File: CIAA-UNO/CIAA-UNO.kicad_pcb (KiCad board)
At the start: 2 copper layers, 53.3 x 68.6 mm, 42 parts, among them CON1 BARREL_JACK, J1 USB_OTG, J2 SWD, P1 Power Header, P2 Analog Header, P3 Digital Header 02, P4 Digital Header 01, Q1 FDN340P, SW1 reset, SW2 reset, U1 LD1117S50TR, U2 LMV358IDGKR, U3 LP2985-33DBVR, U4 USBLC6-2, U5 EFM32HG-48LQFP

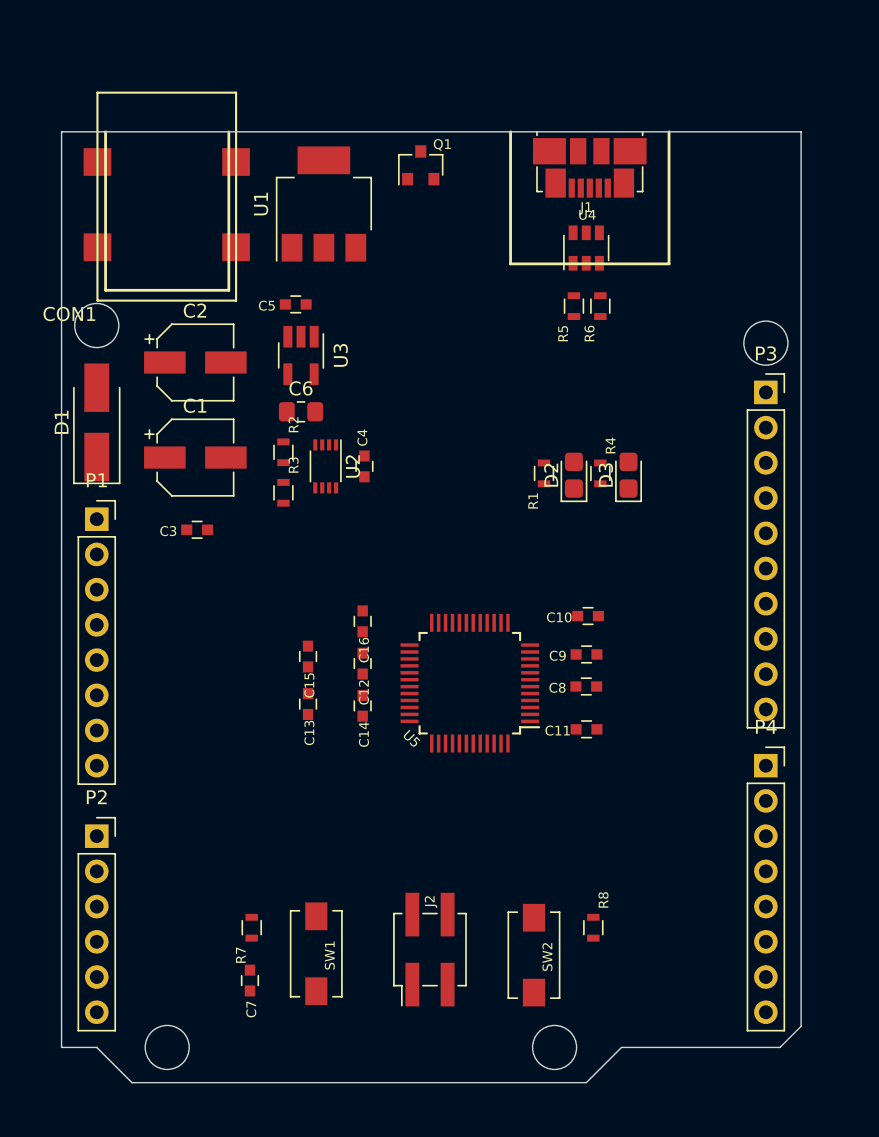
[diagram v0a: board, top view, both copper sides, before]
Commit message: Diseño del PCB
Faltan fiduciales, comentarios y rótulo.
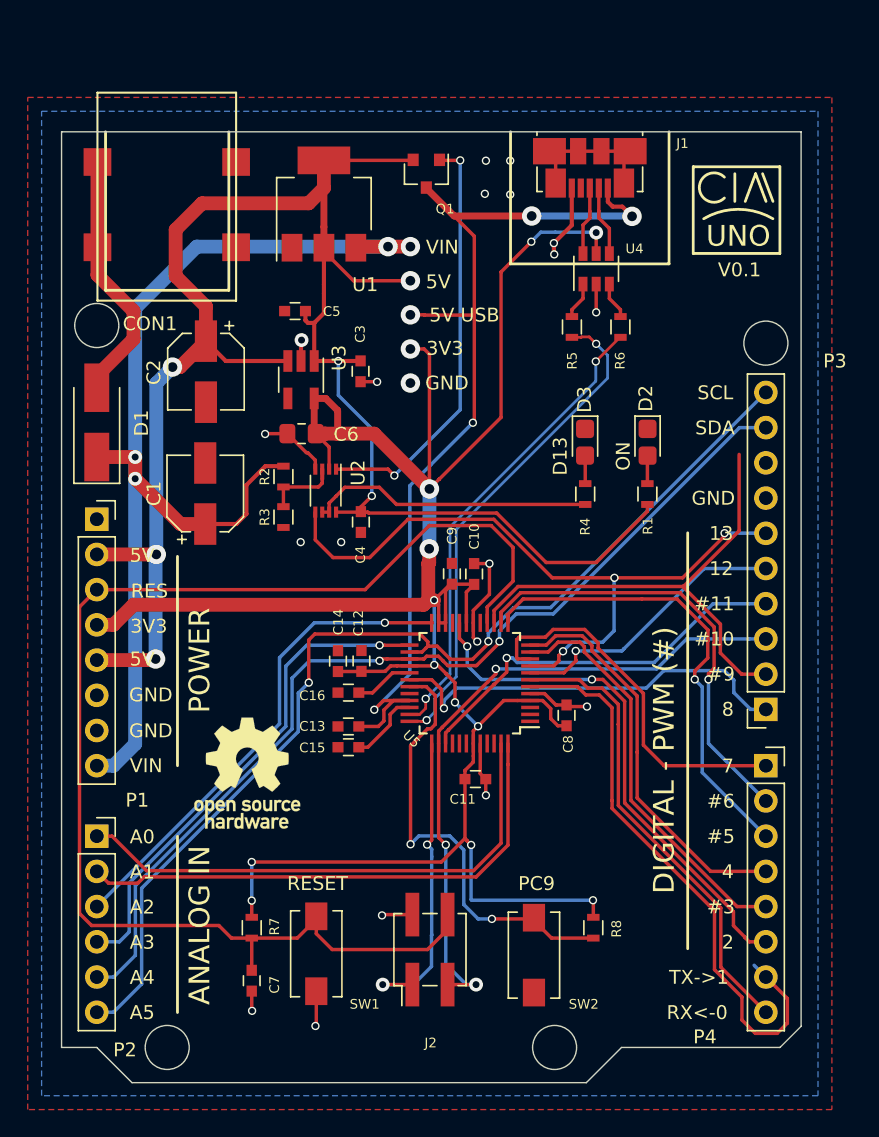
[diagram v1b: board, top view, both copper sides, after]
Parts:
- added REF**: OSHW-Logo_7.5x8mm_SilkScreen, Symbol:OSHW-Logo_7.5x8mm_SilkScreen, F.Cu at (104.8, 76.7)
- moved P3 22.9 mm to (142.2, 72.1), turned to 180 degrees
- moved C3 16.4 mm to (113.0, 47.8), turned to 270 degrees
- moved C9 11.3 mm to (119.6, 62.4), turned to 90 degrees
- moved C11 8.79 mm to (121.3, 77.2), turned to 180 degrees
- moved C10 8.76 mm to (121.2, 62.4), turned to 270 degrees
- moved R1 7.60 mm to (133.7, 56.6)
- moved C15 7.16 mm to (112.1, 74.9), turned to 180 degrees
- moved D2 5.82 mm to (133.7, 52.9), turned to 270 degrees
- moved C16 5.25 mm to (112.1, 70.9), turned to 180 degrees
- moved C4 4.02 mm to (113.0, 58.6), turned to 90 degrees
- moved D3 3.93 mm to (129.2, 52.9), turned to 270 degrees
- moved C14 3.68 mm to (111.4, 68.7)
- moved C13 3.33 mm to (112.1, 73.4), turned to 180 degrees
- moved C1 2.69 mm to (101.8, 56.6), turned to 90 degrees
- moved C8 2.52 mm to (127.9, 72.6), turned to 90 degrees
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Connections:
- P3 pad 2: /EFM32HG-48LQFP/ARD_DIG7 -> /EFM32HG-48LQFP/ARD_DIG9
- U5 pad 10: /EFM32HG-48LQFP/PC4 -> /EFM32HG-48LQFP/ARD_DIG7
- U5 pad 15: /EFM32HG-48LQFP/ARD_DIG7 -> /EFM32HG-48LQFP/ARD_DIG9
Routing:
- net 3V3_LDO: track 0.00 -> 171.6 mm, vias 0 -> 13
- net 5V_LDO: track 0.00 -> 134.2 mm, vias 0 -> 6
- net /EFM32HG-48LQFP/328P_RESET: track 0.00 -> 96.5 mm
- net Vin: track 0.00 -> 78.1 mm, vias 0 -> 4
- net /EFM32HG-48LQFP/ARD_AN5/SCL: track 0.00 -> 77.9 mm, vias 0 -> 2
- net /EFM32HG-48LQFP/ARD_AN4/SDA: track 0.00 -> 70.8 mm, vias 0 -> 2
- net USBVCC: track 0.00 -> 70.4 mm, vias 0 -> 5
- net /EFM32HG-48LQFP/ARD_DIG13/SPI_SCK: track 0.00 -> 50.5 mm, vias 0 -> 3
- net /EFM32HG-48LQFP/ARD_DIG10/SPI_SS: track 0.00 -> 48.4 mm, vias 0 -> 3
- net /EFM32HG-48LQFP/ARD_DIG1: track 0.00 -> 42.1 mm
- net /EFM32HG-48LQFP/ARD_AN1: track 0.00 -> 38.5 mm
- net /EFM32HG-48LQFP/ARD_AN0: track 0.00 -> 38.2 mm
- net /EFM32HG-48LQFP/ARD_DIG2: track 0.00 -> 38.0 mm, vias 0 -> 2
- net GND: track 0.00 -> 37.1 mm, vias 0 -> 20
- net /EFM32HG-48LQFP/ARD_DIG9: track 0.00 -> 36.6 mm
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- added copper zone on B.Cu, net GND
- added copper zone on F.Cu, net GND
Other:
- net class Default: via_dia 0.8 -> 0.6
- board text added: "#10"
- board text added: "#11"
- board text added: "#3"
- board text added: "#5"
- board text added: "#6"
- board text added: "#9"
- board text added: "12"
- board text added: "13"
- board text added: "2"
- board text added: "3V3"
- board text added: "4"
- board text added: "5V"
- board text added: "5V USB"
- board text added: "7"
- board text added: "8"
- board text added: "A0"
- board text added: "A1"
- board text added: "A2"
- board text added: "A3"
- board text added: "A4"
- board text added: "A5"
- board text added: "ANALOG IN"
- board text added: "D13"
- board text added: "DIGITAL - PWM (#)"
- board text added: "GND"
- board text added: "ON"
- board text added: "PC9"
- board text added: "POWER"
- board text added: "RES"
- board text added: "RESET"
- board text added: "RX<-0"
- board text added: "SCL"
- board text added: "SDA"
- board text added: "TX->1"
- board text added: "UNO"
- board text added: "V0.1"
- board text added: "VIN"

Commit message: Modificaciones menores
Se agregó el conector de alimentación, fiduciales y logos. Falta comentarios con datos de fabricación.
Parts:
- removed the REF** at (104.8, 76.7)
- added F1: Fiducial, Fiducial:Fiducial_0.5mm_Dia_1mm_Outer, F.Cu at (133.7, 61.2)
- added F2: Fiducial, Fiducial:Fiducial_0.5mm_Dia_1mm_Outer, F.Cu at (107.3, 96.4)
- added F3: Fiducial, Fiducial:Fiducial_0.5mm_Dia_1mm_Outer, F.Cu at (107.3, 61.2)
- added REF**: OSHW-Logo2_9.8x8mm_SilkScreen, Symbol:OSHW-Logo2_9.8x8mm_SilkScreen, F.Cu at (104.2, 76.3)
- CON1: footprint footprints:barrel jack -> footprints:dc_socket
- moved CON1 5.98 mm to (99.1, 33.2)
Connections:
- CON1 pad 1: GND -> Net-(CON1-Pad1)
- CON1 pad 2: Net-(CON1-Pad2) -> GND
- D1 pad 2: Net-(CON1-Pad2) -> Net-(CON1-Pad1)
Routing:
- net Net-(CON1-Pad2): track 18.5 -> 0.00 mm
- net Net-(CON1-Pad1): track 0.00 -> 11.5 mm
- net GND: track 37.1 -> 44.5 mm
- net 5V_LDO: track 134.2 -> 129.6 mm
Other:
- board text added: "DIG13"
- board text added: "K"
- board text removed: "D13"

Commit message: Detalles finales
Agregados comentarios de fabricación
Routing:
- net GND: track 44.5 -> 43.0 mm, vias 20 -> 19
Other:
- net class Default: clearance 0.2 -> 0.125; via_dia 0.6 -> 0.7
- rule trace_clearance: 0.2 -> 0.125
- board text added: "Ancho de traza 0,125 mm"
- board text added: "Distancia de cobre a borde 0,30 mm"
- board text added: "Diámetro de agujero 0,40 mm"
- board text added: "Diámetro de pad o vía 0,70 mm"
- board text added: "Estándares de fabricación de Mayer"
- board text added: "INDUSTRIA ARGENTINA"
- board text added: "Separación entre traza y pad/vía 0,125 mm"
- board text added: "Separación entre trazas 0,125 mm"

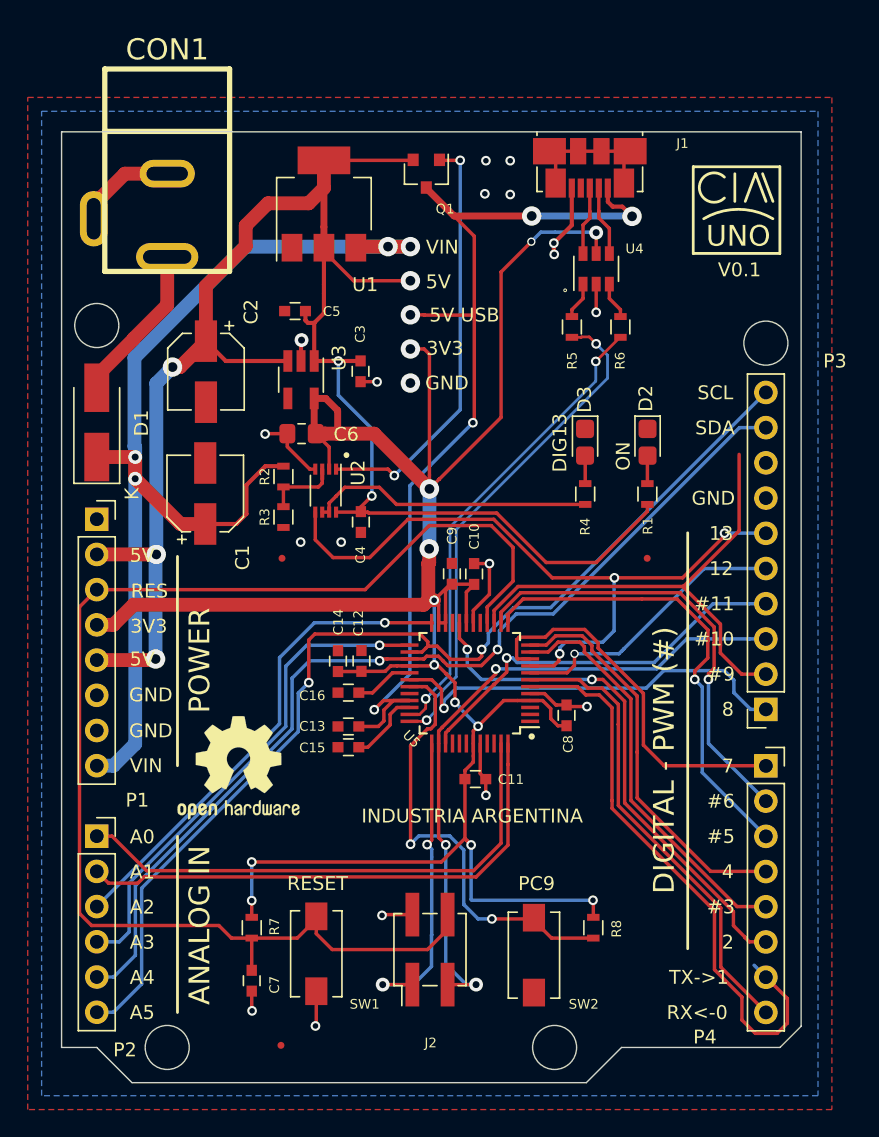
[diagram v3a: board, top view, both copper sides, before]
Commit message: Revisión 2
Se tomaron en  cosideración las correcciones y se modificó para cumplir con las consignas.
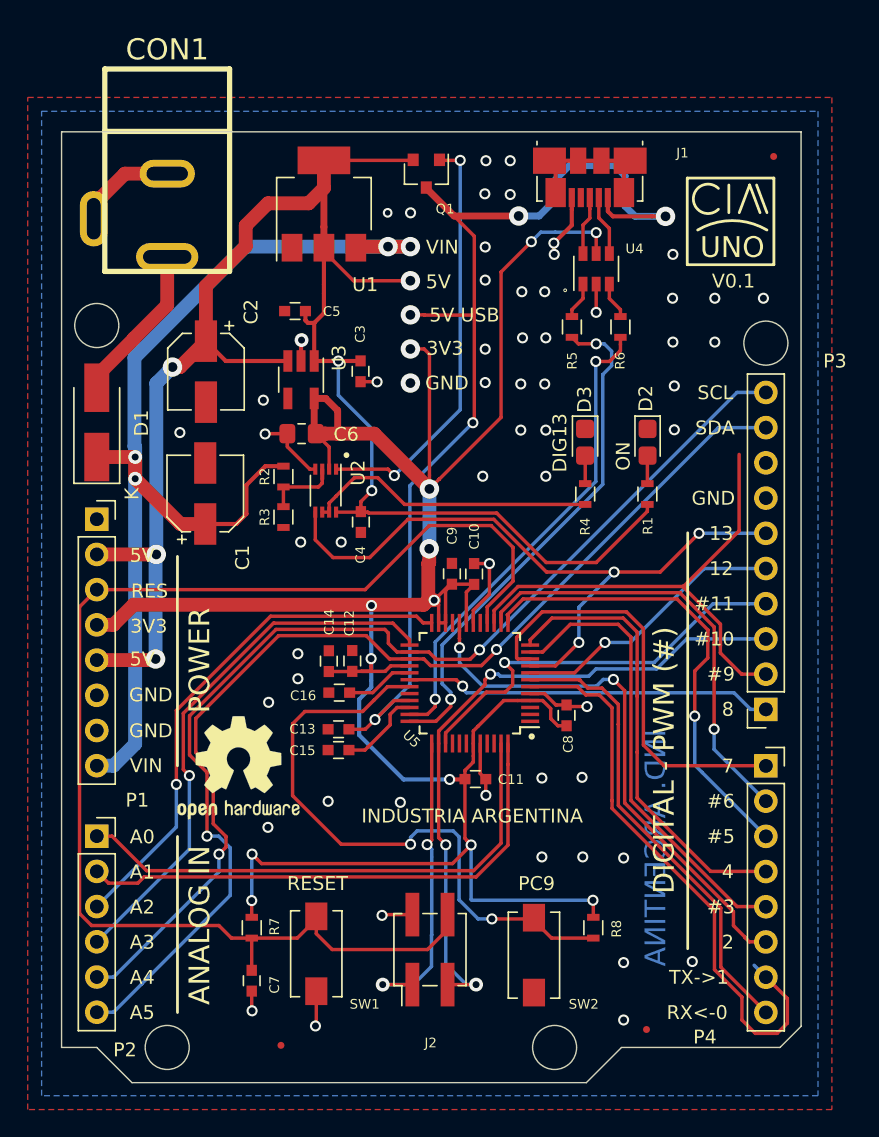
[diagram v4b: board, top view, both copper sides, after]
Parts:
- moved F3 43.0 mm to (133.6, 95.2)
- moved F1 30.4 mm to (142.8, 32.3)
- moved C13 0.74 mm to (111.4, 73.6)
- moved C15 0.74 mm to (111.4, 75.1)
- moved J1 0.69 mm to (129.5, 32.6)
- moved C12 0.66 mm to (112.4, 68.6)
- moved C14 0.66 mm to (110.7, 68.7)
- moved C16 0.66 mm to (111.5, 70.9)
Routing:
- net /EFM32HG-48LQFP/PC9: track 32.7 -> 44.6 mm
- net 3V3_LDO: track 171.6 -> 181.2 mm
- net USBVCC: track 70.4 -> 79.3 mm
- net /EFM32HG-48LQFP/ARD_AN4/SDA: track 71.0 -> 76.0 mm
- net /EFM32HG-48LQFP/ARD_DIG4: track 28.9 -> 32.6 mm
- net /EFM32HG-48LQFP/ARD_DIG8: track 30.4 -> 26.7 mm
- net /EFM32HG-48LQFP/ARD_DIG7: track 27.1 -> 30.7 mm
- net /EFM32HG-48LQFP/ARD_DIG3: track 29.7 -> 33.2 mm
- net /EFM32HG-48LQFP/ARD_AN3: track 36.0 -> 39.3 mm
- net /EFM32HG-48LQFP/ARD_AN5/SCL: track 78.2 -> 81.3 mm
- net /EFM32HG-48LQFP/ARD_AN2: track 35.5 -> 38.0 mm
- net /EFM32HG-48LQFP/USB_D+: track 36.1 -> 37.6 mm
- net /EFM32HG-48LQFP/ARD_DIG13/SPI_SCK: track 50.7 -> 49.3 mm
- net /EFM32HG-48LQFP/ARD_DIG2: track 38.0 -> 39.1 mm
- net /EFM32HG-48LQFP/ARD_DIG11/SPI_MOSI: track 28.6 -> 29.5 mm
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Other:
- net class Default: clearance 0.125 -> 0.2
- rule trace_clearance: 0.125 -> 0.2
- rule trace_min: 0.2 -> 0.25
- board text added: "Ancho de traza 0,250 mm"
- board text added: "Diámetro de agujero 0,50 mm"
- board text added: "Diámetro de pad o vía 0,80 mm"
- board text added: "IND. ARGENTINA"
- board text added: "Separación entre traza y pad/vía 0,2 mm"
- board text added: "Separación entre trazas 0,2 mm"
- board text added: "Tamaños mínimos / Terminación"
- board text added: "Terminación superficial HASL"
